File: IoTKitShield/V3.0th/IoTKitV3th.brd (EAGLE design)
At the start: 97.5 x 58.4 mm, 28 parts, among them J1 4P-2.0, J2 4P-2.0, J3 4P-2.0, J4 4p-2.54

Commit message: Version fuer Produktion
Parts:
- renumbered SPI(V,G,SS,MO,MI,SLK) to SPI(V,G,D9,MO,MI,SLK)
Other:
- board text added: "A0 A1 +5 G"
- board text added: "A5 A4 +5 G"
- board text added: "IoTKit V3, Rev. 1.0, 2018 https://github.com/mc-b/iotkitv3_disco Designed to work with mbed"
- board text removed: "A0 A1 V G"
- board text removed: "A5 A4 V G"
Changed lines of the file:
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@@
 <text x="92.075" y="30.48" size="1.6764" layer="25" rot="R90">A0
 A1
-V
++5
 G</text>
 <text x="92.075" y="22.225" size="1.6764" layer="25" rot="R90">A5
 A4
-V
++5
 G</text>
 <text x="80.01" y="34.29" size="1.6764" layer="25">A5
@@
 +5V
 GND</text>
-<text x="19.05" y="25.4" size="1.6764" layer="25">D3~
+<text x="19.685" y="26.035" size="1.6764" layer="25">D3~
 D5~
 D6~
 D9~</text>
-<text x="19.05" y="35.56" size="1.6764" layer="25" rot="R90">GND
+<text x="18.415" y="36.195" size="1.6764" layer="25" rot="R90">GND
 +5V
 S</text>
@@
 D7</text>
 <wire x1="24.13" y1="57.15" x2="24.13" y2="41.91" width="0.1524" layer="25"/>
-<wire x1="24.13" y1="41.91" x2="22.86" y2="40.64" width="0.1524" layer="25"/>
-<wire x1="22.86" y1="40.64" x2="8.89" y2="40.64" width="0.1524" layer="25"/>
-<wire x1="8.89" y1="40.64" x2="7.62" y2="41.91" width="0.1524" layer="25"/>
+<wire x1="24.13" y1="41.91" x2="23.495" y2="41.275" width="0.1524" layer="25"/>
+<wire x1="23.495" y1="41.275" x2="8.89" y2="41.275" width="0.1524" layer="25"/>
+<wire x1="8.89" y1="41.275" x2="7.62" y2="41.91" width="0.1524" layer="25"/>
 <wire x1="7.62" y1="41.91" x2="7.62" y2="52.07" width="0.1524" layer="25"/>
 <wire x1="7.62" y1="52.07" x2="7.62" y2="57.15" width="0.1524" layer="25"/>
@@
 GND</text>
 <text x="10.16" y="13.335" size="1.6764" layer="25">I2C</text>
-<text x="19.685" y="20.32" size="1.6764" layer="25" rot="R90">D9
+<text x="20.32" y="20.955" size="1.6764" layer="25" rot="R90">D9
 D10
 +5V
@@
 <wire x1="53.34" y1="45.72" x2="54.61" y2="44.45" width="0.1524" layer="25"/>
 <text x="55.88" y="50.8" size="1.778" layer="25">A3</text>
+<text x="69.85" y="46.99" size="1.778" layer="26" rot="MR0">IoTKit V3, Rev. 1.0, 2018
+https://github.com/mc-b/iotkitv3_disco
+Designed to work with mbed</text>
 </plain>
 <attributes>
@@
 <attribute name="VALUE" x="91.44" y="41.275" size="1.27" layer="27" rot="R180"/>
 </element>
-<element name="SPI(V,G,SS,MO,MI,SLK)" library="pinhead" package="1X06" value="" x="5.08" y="41.91" rot="R90">
+<element name="SPI(V,G,D9,MO,MI,SLK)" library="pinhead" package="1X06" value="" x="5.08" y="41.91" rot="R90">
 <attribute name="NAME" x="3.2512" y="29.1338" size="1.6764" layer="25" ratio="10" rot="R90"/>
 <attribute name="VALUE" x="8.255" y="34.29" size="1.27" layer="27" rot="R90"/>
@@
 <contactref element="B1" pad="D9"/>
 <contactref element="STEPPER" pad="4"/>
-<contactref element="SPI(V,G,SS,MO,MI,SLK)" pad="3"/>
+<contactref element="SPI(V,G,D9,MO,MI,SLK)" pad="3"/>
 <contactref element="D6" pad="5"/>
 <wire x1="35.5092" y1="34.8996" x2="35.5092" y2="35.5092" width="0.1524" layer="16"/>
@@
 <signal name="D11">
 <contactref element="B1" pad="D11"/>
-<contactref element="SPI(V,G,SS,MO,MI,SLK)" pad="4"/>
+<contactref element="SPI(V,G,D9,MO,MI,SLK)" pad="4"/>
 <contactref element="NFC/RFID" pad="4"/>
 <wire x1="5.0292" y1="15.5448" x2="5.0292" y2="15.24" width="0.1524" layer="1"/>
@@
 <signal name="D12">
 <contactref element="B1" pad="D12"/>
-<contactref element="SPI(V,G,SS,MO,MI,SLK)" pad="5"/>
+<contactref element="SPI(V,G,D9,MO,MI,SLK)" pad="5"/>
 <contactref element="NFC/RFID" pad="3"/>
 <wire x1="5.0292" y1="13.1064" x2="5.0292" y2="12.8016" width="0.1524" layer="16"/>
@@
 <signal name="D13">
 <contactref element="B1" pad="D13"/>
-<contactref element="SPI(V,G,SS,MO,MI,SLK)" pad="6"/>
+<contactref element="SPI(V,G,D9,MO,MI,SLK)" pad="6"/>
 <contactref element="NFC/RFID" pad="2"/>
 <wire x1="5.0292" y1="9.7536" x2="5.0292" y2="10.0584" width="0.1524" layer="1"/>
@@
 <contactref element="H-BRIDGE" pad="16"/>
 <contactref element="H-BRIDGE" pad="8"/>
-<contactref element="SPI(V,G,SS,MO,MI,SLK)" pad="2"/>
+<contactref element="SPI(V,G,D9,MO,MI,SLK)" pad="2"/>
 <contactref element="R3" pad="1"/>
 <contactref element="R2" pad="1"/>
@@
 <contactref element="UART(D0/D1)" pad="4"/>
 <contactref element="J4" pad="4"/>
-<contactref element="SPI(V,G,SS,MO,MI,SLK)" pad="1"/>
+<contactref element="SPI(V,G,D9,MO,MI,SLK)" pad="1"/>
 <contactref element="OLED(0X78)" pad="1"/>
 <contactref element="NFC/RFID" pad="6"/>

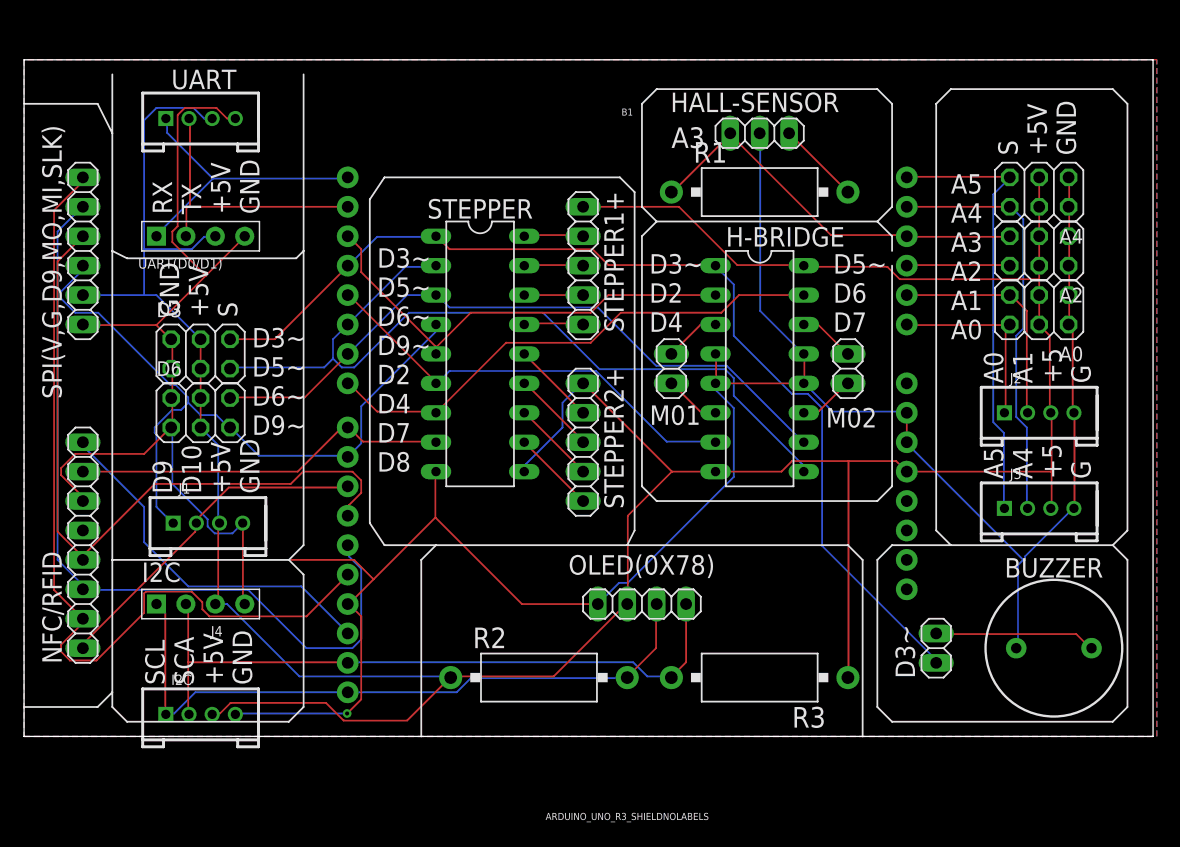
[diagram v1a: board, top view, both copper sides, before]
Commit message: Textkorrekturen
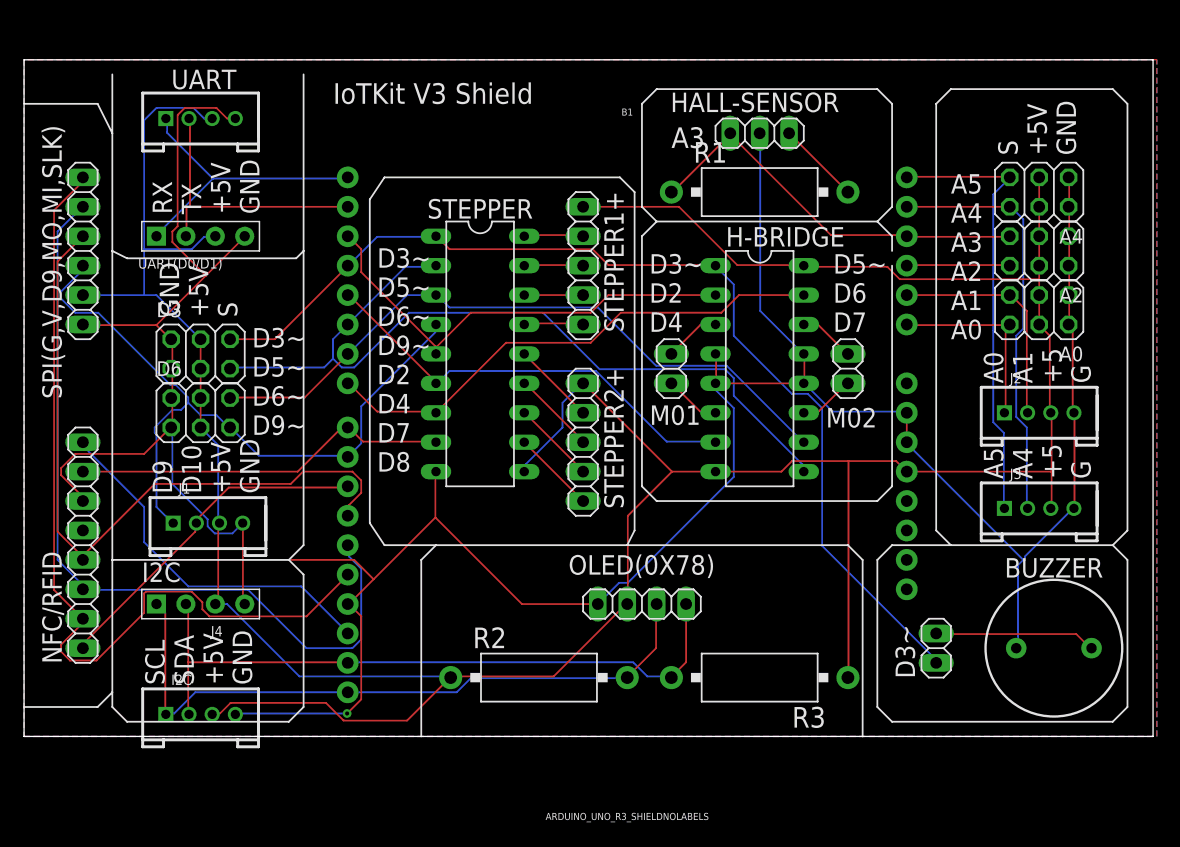
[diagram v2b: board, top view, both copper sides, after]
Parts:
- renumbered SPI(V,G,D9,MO,MI,SLK) to SPI(G,V,D9,MO,MI,SLK)
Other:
- board text added: "IoTKit V3 Shield"
- board text added: "SCL SDA +5V GND"
- board text removed: "SCL SCA +5V GND"
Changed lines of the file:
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@@
 <wire x1="7.62" y1="2.54" x2="7.62" y2="3.81" width="0.1524" layer="25"/>
 <text x="19.685" y="4.445" size="1.6764" layer="25" rot="R90">SCL
-SCA
+SDA
 +5V
 GND</text>
@@
 https://github.com/mc-b/iotkitv3_disco
 Designed to work with mbed</text>
+<text x="26.67" y="54.61" size="1.778" layer="25">IoTKit V3 Shield</text>
 </plain>
 <attributes>
@@
 <attribute name="VALUE" x="91.44" y="41.275" size="1.27" layer="27" rot="R180"/>
 </element>
-<element name="SPI(V,G,D9,MO,MI,SLK)" library="pinhead" package="1X06" value="" x="5.08" y="41.91" rot="R90">
+<element name="SPI(G,V,D9,MO,MI,SLK)" library="pinhead" package="1X06" value="" x="5.08" y="41.91" rot="R90">
 <attribute name="NAME" x="3.2512" y="29.1338" size="1.6764" layer="25" ratio="10" rot="R90"/>
 <attribute name="VALUE" x="8.255" y="34.29" size="1.27" layer="27" rot="R90"/>
@@
 <contactref element="B1" pad="D9"/>
 <contactref element="STEPPER" pad="4"/>
-<contactref element="SPI(V,G,D9,MO,MI,SLK)" pad="3"/>
+<contactref element="SPI(G,V,D9,MO,MI,SLK)" pad="3"/>
 <contactref element="D6" pad="5"/>
 <wire x1="35.5092" y1="34.8996" x2="35.5092" y2="35.5092" width="0.1524" layer="16"/>
@@
 <signal name="D11">
 <contactref element="B1" pad="D11"/>
-<contactref element="SPI(V,G,D9,MO,MI,SLK)" pad="4"/>
+<contactref element="SPI(G,V,D9,MO,MI,SLK)" pad="4"/>
 <contactref element="NFC/RFID" pad="4"/>
 <wire x1="5.0292" y1="15.5448" x2="5.0292" y2="15.24" width="0.1524" layer="1"/>
@@
 <signal name="D12">
 <contactref element="B1" pad="D12"/>
-<contactref element="SPI(V,G,D9,MO,MI,SLK)" pad="5"/>
+<contactref element="SPI(G,V,D9,MO,MI,SLK)" pad="5"/>
 <contactref element="NFC/RFID" pad="3"/>
 <wire x1="5.0292" y1="13.1064" x2="5.0292" y2="12.8016" width="0.1524" layer="16"/>
@@
 <signal name="D13">
 <contactref element="B1" pad="D13"/>
-<contactref element="SPI(V,G,D9,MO,MI,SLK)" pad="6"/>
+<contactref element="SPI(G,V,D9,MO,MI,SLK)" pad="6"/>
 <contactref element="NFC/RFID" pad="2"/>
 <wire x1="5.0292" y1="9.7536" x2="5.0292" y2="10.0584" width="0.1524" layer="1"/>
@@
 <contactref element="H-BRIDGE" pad="16"/>
 <contactref element="H-BRIDGE" pad="8"/>
-<contactref element="SPI(V,G,D9,MO,MI,SLK)" pad="2"/>
+<contactref element="SPI(G,V,D9,MO,MI,SLK)" pad="2"/>
 <contactref element="R3" pad="1"/>
 <contactref element="R2" pad="1"/>
@@
 <contactref element="UART(D0/D1)" pad="4"/>
 <contactref element="J4" pad="4"/>
-<contactref element="SPI(V,G,D9,MO,MI,SLK)" pad="1"/>
+<contactref element="SPI(G,V,D9,MO,MI,SLK)" pad="1"/>
 <contactref element="OLED(0X78)" pad="1"/>
 <contactref element="NFC/RFID" pad="6"/>

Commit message: Korrekturen NFC, Hallsensor, Servos
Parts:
- removed SPI(G,V,D9,MO,MI,SLK): (no value), pinhead:1X06
- added SPI: (no value), pinhead:1X06
- moved NFC/RFID 2.84 mm to (3.81, 14.0)
- moved I2C 1.42 mm to (15.9, 3.17)
- moved J4 0.90 mm to (15.9, 12.1)
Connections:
- removed net N$13: HALL-SENSOR.3, R1.2
- net +3V3: now also HALL-SENSOR.3, R1.1
- net +5V: now also SPI.2; no longer SPI(G,V,D9,MO,MI,SLK).2
- net A3: now also R1.2; no longer R1.1
- net D10: now also D6.6
- net D11: now also D6.5, NFC/RFID.3, SPI.4; no longer NFC/RFID.4, SPI(G,V,D9,MO,MI,SLK).4
- net D12: now also NFC/RFID.4, SPI.5; no longer NFC/RFID.3, SPI(G,V,D9,MO,MI,SLK).5
- net D13: now also SPI.6; no longer SPI(G,V,D9,MO,MI,SLK).6
- net D3: no longer D3.6
- net D5: no longer D3.5
- net D6: now also D3.6; no longer D6.6
- net D9: now also D3.5, SPI.3; no longer D6.5, SPI(G,V,D9,MO,MI,SLK).3
- net GND: now also SPI.1; no longer SPI(G,V,D9,MO,MI,SLK).1
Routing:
- net +5V: track 285.8 -> 0.00 mm
- net GND: track 275.5 -> 0.00 mm, vias 1 -> 0
- net D3: track 89.6 -> 0.00 mm
- net D13: track 75.0 -> 0.00 mm
- net D5: track 72.3 -> 0.00 mm
- net D12: track 69.9 -> 0.00 mm
- net D9: track 61.6 -> 0.00 mm
- net D11: track 61.1 -> 0.00 mm
- net SDA: track 58.8 -> 0.00 mm
- net D6: track 58.5 -> 0.00 mm
- net SCL: track 58.4 -> 0.00 mm
- net D7: track 44.7 -> 0.00 mm
- net D2: track 39.9 -> 0.00 mm
- net A5: track 38.5 -> 0.00 mm
- net D4: track 38.1 -> 0.00 mm
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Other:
- board text added: "+"
- board text added: "+3V3 RST (D8) GND IRQ (NC) MISO (D12) MOSI (D11) SCLK (D13) CS (D10)"
- board text added: "D6~ D9~ D10~ D11~"
- board text added: "SCLK (D13) MISO (D12) MOSI (D11) SS (D9) +5V GND"
- board text removed: "D3~ D5~ D6~ D9~"
